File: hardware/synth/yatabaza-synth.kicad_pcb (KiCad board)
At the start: 2 copper layers, 46.4 x 60.3 mm, 32 parts, among them P1 Φ, P2 BUS, P3 POWER, P4 AUDIO, U1 MCP23017, U2 YM3812, U3 74HC14, U4 YM3014B, U5 NE5532, Y1 3.58MHz

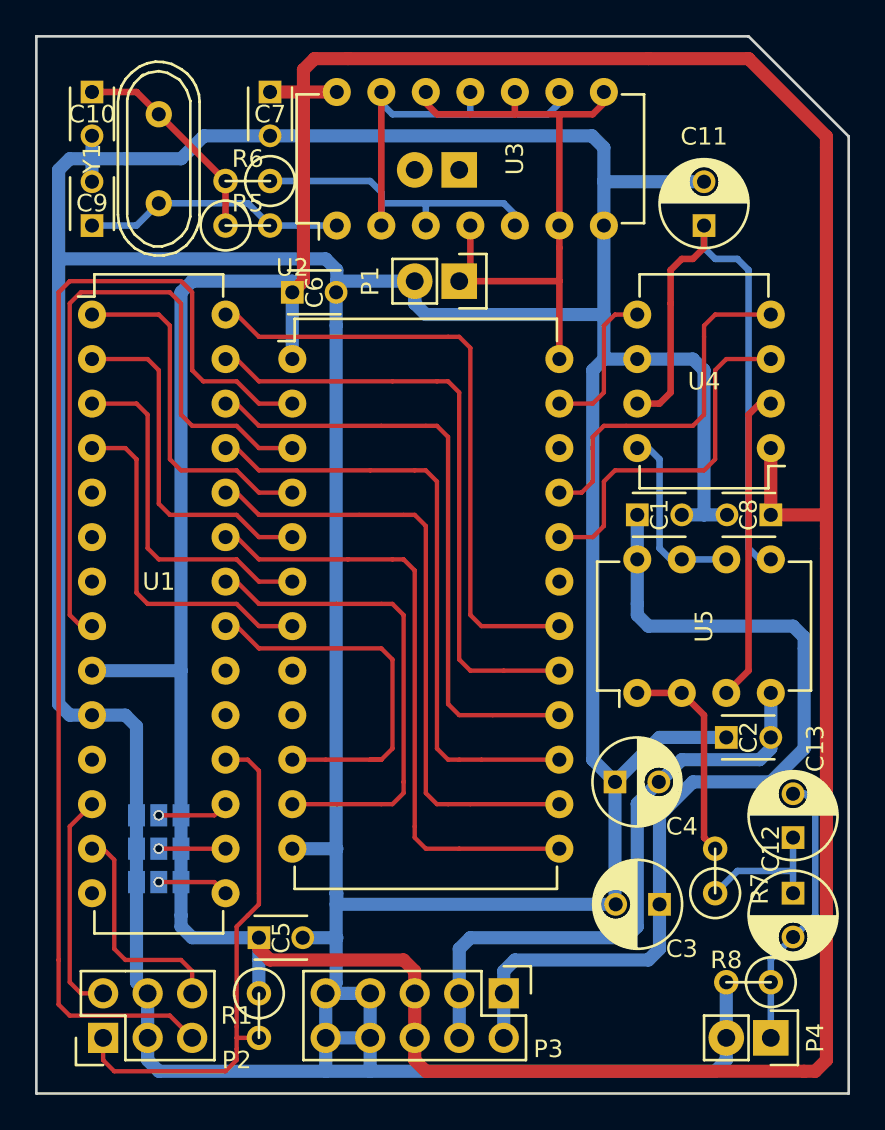
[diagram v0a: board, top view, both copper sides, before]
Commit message: ~ Ported hardware to Kicad6
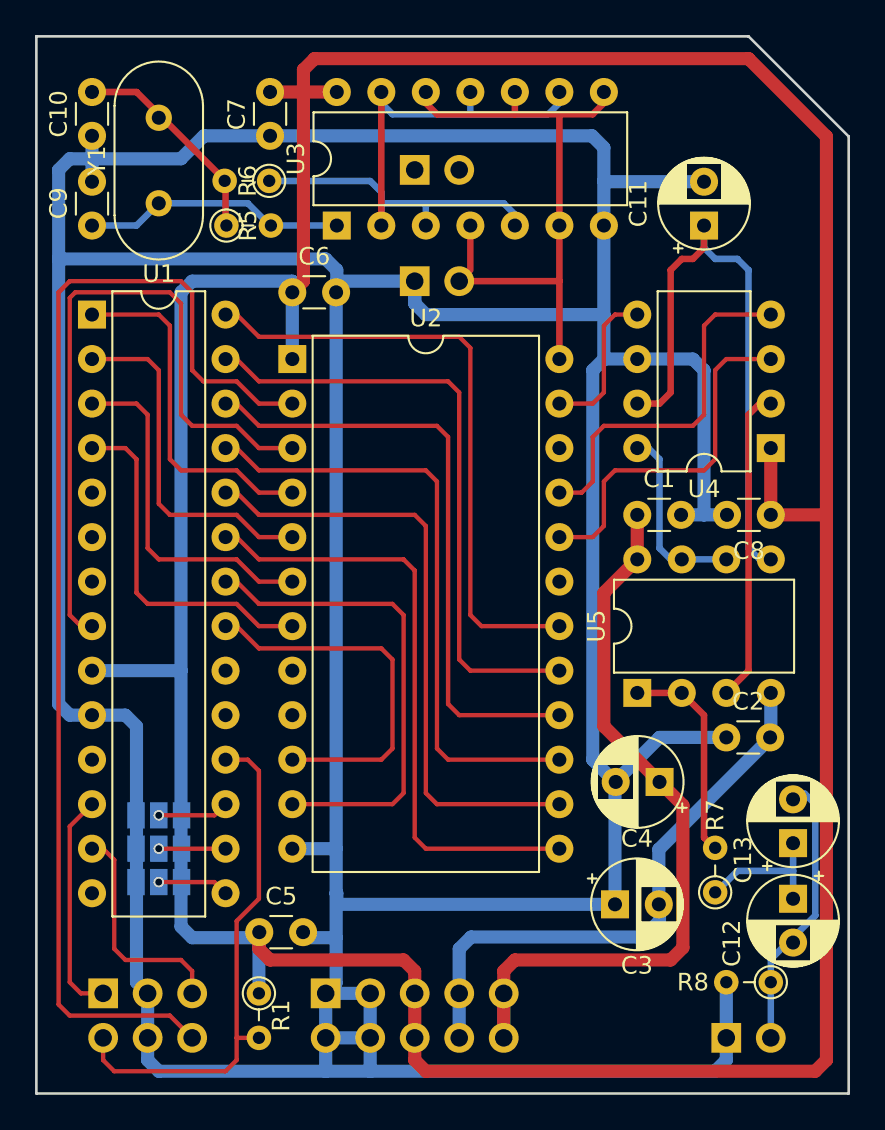
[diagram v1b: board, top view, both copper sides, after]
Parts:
- ?: value Pin_Header_Straight_1x02 -> PinHeader_1x02_P2.54mm_Vertical; footprint Pin_Headers:Pin_Header_Straight_1x02 -> Connector_PinHeader_2.54mm:PinHeader_1x02_P2.54mm_Vertical
- A0, A1, A2: footprint Connect:GS3 -> Jumper:SolderJumper-3_P1.3mm_Open_Pad1.0x1.5mm_NumberLabels
- C1, C10, C2, C5, C6, C7, C8, C9: footprint Capacitors_ThroughHole:C_Disc_D3_P2.5 -> Capacitor_THT:C_Disc_D3.0mm_W1.6mm_P2.50mm
- C11, C12, C13, C3, C4: footprint Capacitors_ThroughHole:C_Radial_D5_L6_P2.5 -> Capacitor_THT:CP_Radial_D5.0mm_P2.50mm
- P1, P4: footprint Pin_Headers:Pin_Header_Straight_1x02 -> Connector_PinHeader_2.54mm:PinHeader_1x02_P2.54mm_Vertical; moved to B.Cu
- P2: footprint Pin_Headers:Pin_Header_Straight_2x03 -> Connector_PinHeader_2.54mm:PinHeader_2x03_P2.54mm_Vertical; moved to B.Cu
- P3: footprint Pin_Headers:Pin_Header_Straight_2x05 -> Connector_PinHeader_2.54mm:PinHeader_2x05_P2.54mm_Vertical; moved to B.Cu
- R1, R5, R6, R7, R8: footprint Discret:R1 -> Resistor_THT:R_Axial_DIN0204_L3.6mm_D1.6mm_P2.54mm_Vertical
- U1: footprint Housings_DIP:DIP-28_W7.62mm -> Package_DIP:DIP-28_W7.62mm
- U2: footprint Housings_DIP:DIP-24_W15.24mm -> Package_DIP:DIP-24_W15.24mm
- U3: footprint Housings_DIP:DIP-14_W7.62mm -> Package_DIP:DIP-14_W7.62mm
- U4, U5: footprint Housings_DIP:DIP-8_W7.62mm -> Package_DIP:DIP-8_W7.62mm
- Y1: footprint Crystals:Crystal_HC49-U_Vertical -> Crystal:Crystal_HC49-U_Vertical
- moved P3 10.2 mm to (31.1, 66.7)
- moved C3 6.98 mm to (50.2, 54.6)
- moved C4 6.98 mm to (47.6, 61.6)
- moved P2 2.54 mm to (18.4, 66.7), turned to -90 degrees
- moved ? 2.54 mm to (36.2, 19.7), turned to -90 degrees
- moved P1 2.54 mm to (36.2, 26.0)
- moved P4 2.54 mm to (54.0, 69.2)
- moved Y1 2.54 mm to (21.6, 21.6)
- moved R8 1.27 mm to (56.5, 66.0)
- moved R1 1.27 mm to (27.3, 66.7)
- moved R6 1.22 mm to (27.9, 20.3)
- moved R5 1.22 mm to (25.4, 22.9)
- moved R7 1.22 mm to (53.3, 60.9)
- moved C5 0.32 mm to (27.3, 63.2)
- moved C12 0.32 mm to (57.8, 61.3)
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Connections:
- P1 pad 1: /Φ -> GND
- P1 pad 2: GND -> /Φ
- P2 pad 1: /~RST -> /SCL
- P2 pad 2: /SCL -> /~{RST}
- P2 pad 5: /~IRQ -> /SDA
- P2 pad 6: /SDA -> /~{IRQ}
- P3 pad 1: +9VA -> GND
- P3 pad 10: GND -> +9VA
- P3 pad 2: +9VA -> GND
- P3 pad 3: -9VA -> GND
- P3 pad 4: -9VA -> GND
- P3 pad 7: GND -> -9VA
- P3 pad 8: GND -> -9VA
- P3 pad 9: GND -> +9VA
- P4 pad 1: Net-(C12-Pad2) -> GND
- P4 pad 2: GND -> Net-(C12-Pad2)
- R1 pad 2: /~RST -> /~{RST}
- U1 pad 11: (no net) -> unconnected-(U1-Pad11)
- U1 pad 14: (no net) -> unconnected-(U1-Pad14)
- U1 pad 18: /~RST -> /~{RST}
- U1 pad 19: Net-(U1-Pad19) -> unconnected-(U1-Pad19)
- U1 pad 20: Net-(U1-Pad20) -> unconnected-(U1-Pad20)
- U1 pad 5: Net-(U1-Pad5) -> unconnected-(U1-Pad5)
- U1 pad 6: Net-(U1-Pad6) -> unconnected-(U1-Pad6)
- U1 pad 7: Net-(U1-Pad7) -> unconnected-(U1-Pad7)
- U2 pad 2: /~IRQ -> /~{IRQ}
- U2 pad 8: (no net) -> unconnected-(U2-Pad8)
- U2 pad 9: (no net) -> unconnected-(U2-Pad9)
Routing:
- net /~{IRQ}: track 0.00 -> 68.1 mm
- net /~IRQ: track 68.1 -> 0.00 mm
- net /~{RST}: track 0.00 -> 29.9 mm
- net /~RST: track 29.9 -> 0.00 mm
- net +9VA: track 52.8 -> 44.5 mm
- net -9VA: track 34.9 -> 32.8 mm
- net Net-(U1-Pad28): track 36.0 -> 34.7 mm
- net Net-(U1-Pad21): track 22.0 -> 20.7 mm
- net /Φ: track 36.3 -> 35.5 mm
- net Net-(U2-Pad23): track 9.42 -> 8.78 mm
- net Net-(U1-Pad27): track 35.3 -> 34.7 mm
- net Net-(U1-Pad26): track 35.3 -> 34.7 mm
- net Net-(U1-Pad25): track 35.3 -> 34.7 mm
- net Net-(U1-Pad24): track 35.3 -> 34.7 mm
- net Net-(U1-Pad22): track 27.7 -> 27.1 mm
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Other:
- net class Default removed
- rule pad_to_mask_clearance: 0.2 -> 0
